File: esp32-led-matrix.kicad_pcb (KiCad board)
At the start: 2 copper layers, 20.5 x 35.5 mm, 20 parts, among them J1 Conn_01x03, J2 Conn_01x03, J4 USB_C_Receptacle_USB2.0_16P, SW1 RESET, U1 ESP32-C6-WROOM-1, U2 USBLC6-2SC6, U3 LM1117DT-3.3

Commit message: process
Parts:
- removed J1: Conn_01x03, Connector_PinHeader_2.54mm:PinHeader_1x03_P2.54mm_Vertical
- added D10: WS2812B, PCM_SparkFun-LED:WS2812_2020, F.Cu at (7.25, 4.00)
- added D100: WS2812B, PCM_SparkFun-LED:WS2812_2020, B.Cu at (29.8, 17.5)
- added D101: WS2812B, PCM_SparkFun-LED:WS2812_2020, B.Cu at (25.2, 17.5)
- added D102: WS2812B, PCM_SparkFun-LED:WS2812_2020, B.Cu at (20.8, 17.5)
- added D103: WS2812B, PCM_SparkFun-LED:WS2812_2020, B.Cu at (16.2, 17.5)
- added D104: WS2812B, PCM_SparkFun-LED:WS2812_2020, B.Cu at (11.8, 17.5)
- added D105: WS2812B, PCM_SparkFun-LED:WS2812_2020, B.Cu at (7.25, 17.5)
- added D106: WS2812B, PCM_SparkFun-LED:WS2812_2020, B.Cu at (7.25, 22.0)
- added D107: WS2812B, PCM_SparkFun-LED:WS2812_2020, B.Cu at (11.8, 22.0)
- added D108: WS2812B, PCM_SparkFun-LED:WS2812_2020, B.Cu at (16.2, 22.0)
- added D109: WS2812B, PCM_SparkFun-LED:WS2812_2020, B.Cu at (20.8, 22.0)
- added D11: WS2812B, PCM_SparkFun-LED:WS2812_2020, F.Cu at (11.8, 4.00)
- added D110: WS2812B, PCM_SparkFun-LED:WS2812_2020, B.Cu at (25.2, 22.0)
- added D111: WS2812B, PCM_SparkFun-LED:WS2812_2020, B.Cu at (29.8, 22.0)
- added D112: WS2812B, PCM_SparkFun-LED:WS2812_2020, B.Cu at (34.2, 22.0)
- added D113: WS2812B, PCM_SparkFun-LED:WS2812_2020, B.Cu at (38.8, 22.0)
- added D114: WS2812B, PCM_SparkFun-LED:WS2812_2020, B.Cu at (38.8, 26.5)
- added D115: WS2812B, PCM_SparkFun-LED:WS2812_2020, B.Cu at (34.2, 26.5)
- added D116: WS2812B, PCM_SparkFun-LED:WS2812_2020, B.Cu at (29.8, 26.5)
- added D117: WS2812B, PCM_SparkFun-LED:WS2812_2020, B.Cu at (25.2, 26.5)
- added D118: WS2812B, PCM_SparkFun-LED:WS2812_2020, B.Cu at (20.8, 26.5)
- added D119: WS2812B, PCM_SparkFun-LED:WS2812_2020, B.Cu at (16.2, 26.5)
- added D12: WS2812B, PCM_SparkFun-LED:WS2812_2020, F.Cu at (16.2, 4.00)
- added D120: WS2812B, PCM_SparkFun-LED:WS2812_2020, B.Cu at (11.8, 26.5)
- added D121: WS2812B, PCM_SparkFun-LED:WS2812_2020, B.Cu at (7.25, 26.5)
- added D122: WS2812B, PCM_SparkFun-LED:WS2812_2020, B.Cu at (7.25, 31.0)
- added D123: WS2812B, PCM_SparkFun-LED:WS2812_2020, B.Cu at (11.8, 31.0)
- added D124: WS2812B, PCM_SparkFun-LED:WS2812_2020, B.Cu at (16.2, 31.0)
- added D125: WS2812B, PCM_SparkFun-LED:WS2812_2020, B.Cu at (20.8, 31.0)
- added D126: WS2812B, PCM_SparkFun-LED:WS2812_2020, B.Cu at (25.2, 31.0)
- added D127: WS2812B, PCM_SparkFun-LED:WS2812_2020, B.Cu at (29.8, 31.0)
- added D128: WS2812B, PCM_SparkFun-LED:WS2812_2020, B.Cu at (34.2, 31.0)
- added D129: WS2812B, PCM_SparkFun-LED:WS2812_2020, B.Cu at (38.8, 31.0)
- added D13: WS2812B, PCM_SparkFun-LED:WS2812_2020, F.Cu at (20.8, 4.00)
- added D130: WS2812B, PCM_SparkFun-LED:WS2812_2020, B.Cu at (38.8, 35.5)
- added D131: WS2812B, PCM_SparkFun-LED:WS2812_2020, B.Cu at (34.2, 35.5)
- added D132: WS2812B, PCM_SparkFun-LED:WS2812_2020, B.Cu at (29.8, 35.5)
- added D133: WS2812B, PCM_SparkFun-LED:WS2812_2020, B.Cu at (25.2, 35.5)
- added D134: WS2812B, PCM_SparkFun-LED:WS2812_2020, B.Cu at (20.8, 35.5)
- added D135: WS2812B, PCM_SparkFun-LED:WS2812_2020, B.Cu at (16.2, 35.5)
- added D136: WS2812B, PCM_SparkFun-LED:WS2812_2020, B.Cu at (11.8, 35.5)
- added D137: WS2812B, PCM_SparkFun-LED:WS2812_2020, B.Cu at (7.25, 35.5)
- added D14: WS2812B, PCM_SparkFun-LED:WS2812_2020, F.Cu at (25.2, 4.00)
- added D15: WS2812B, PCM_SparkFun-LED:WS2812_2020, F.Cu at (29.8, 4.00)
- added D16: WS2812B, PCM_SparkFun-LED:WS2812_2020, F.Cu at (34.2, 4.00)
- added D17: WS2812B, PCM_SparkFun-LED:WS2812_2020, F.Cu at (38.8, 4.00)
- added D18: WS2812B, PCM_SparkFun-LED:WS2812_2020, F.Cu at (38.8, 8.50)
- added D19: WS2812B, PCM_SparkFun-LED:WS2812_2020, F.Cu at (34.2, 8.50)
- added D20: WS2812B, PCM_SparkFun-LED:WS2812_2020, F.Cu at (29.8, 8.50)
- added D21: WS2812B, PCM_SparkFun-LED:WS2812_2020, F.Cu at (25.2, 8.50)
- added D22: WS2812B, PCM_SparkFun-LED:WS2812_2020, F.Cu at (20.8, 8.50)
- added D23: WS2812B, PCM_SparkFun-LED:WS2812_2020, F.Cu at (16.2, 8.50)
- added D24: WS2812B, PCM_SparkFun-LED:WS2812_2020, F.Cu at (11.8, 8.50)
- added D25: WS2812B, PCM_SparkFun-LED:WS2812_2020, F.Cu at (7.25, 8.50)
- added D26: WS2812B, PCM_SparkFun-LED:WS2812_2020, F.Cu at (7.25, 13.0)
- added D27: WS2812B, PCM_SparkFun-LED:WS2812_2020, F.Cu at (11.8, 13.0)
- added D28: WS2812B, PCM_SparkFun-LED:WS2812_2020, F.Cu at (16.2, 13.0)
- added D29: WS2812B, PCM_SparkFun-LED:WS2812_2020, F.Cu at (20.8, 13.0)
- added D30: WS2812B, PCM_SparkFun-LED:WS2812_2020, F.Cu at (25.2, 13.0)
- added D31: WS2812B, PCM_SparkFun-LED:WS2812_2020, F.Cu at (29.8, 13.0)
- added D32: WS2812B, PCM_SparkFun-LED:WS2812_2020, F.Cu at (34.2, 13.0)
- added D33: WS2812B, PCM_SparkFun-LED:WS2812_2020, F.Cu at (38.8, 13.0)
- added D34: WS2812B, PCM_SparkFun-LED:WS2812_2020, F.Cu at (38.8, 17.5)
- added D35: WS2812B, PCM_SparkFun-LED:WS2812_2020, F.Cu at (34.2, 17.5)
- added D36: WS2812B, PCM_SparkFun-LED:WS2812_2020, F.Cu at (29.8, 17.5)
- added D37: WS2812B, PCM_SparkFun-LED:WS2812_2020, F.Cu at (25.2, 17.5)
- added D38: WS2812B, PCM_SparkFun-LED:WS2812_2020, F.Cu at (20.8, 17.5)
- added D39: WS2812B, PCM_SparkFun-LED:WS2812_2020, F.Cu at (16.2, 17.5)
- added D40: WS2812B, PCM_SparkFun-LED:WS2812_2020, F.Cu at (11.8, 17.5)
- added D41: WS2812B, PCM_SparkFun-LED:WS2812_2020, F.Cu at (7.25, 17.5)
- added D42: WS2812B, PCM_SparkFun-LED:WS2812_2020, F.Cu at (7.25, 22.0)
- added D43: WS2812B, PCM_SparkFun-LED:WS2812_2020, F.Cu at (11.8, 22.0)
- added D44: WS2812B, PCM_SparkFun-LED:WS2812_2020, F.Cu at (16.2, 22.0)
- added D45: WS2812B, PCM_SparkFun-LED:WS2812_2020, F.Cu at (20.8, 22.0)
- added D46: WS2812B, PCM_SparkFun-LED:WS2812_2020, F.Cu at (25.2, 22.0)
- added D47: WS2812B, PCM_SparkFun-LED:WS2812_2020, F.Cu at (29.8, 22.0)
- added D48: WS2812B, PCM_SparkFun-LED:WS2812_2020, F.Cu at (34.2, 22.0)
- added D49: WS2812B, PCM_SparkFun-LED:WS2812_2020, F.Cu at (38.8, 22.0)
- added D50: WS2812B, PCM_SparkFun-LED:WS2812_2020, F.Cu at (38.8, 26.5)
- added D51: WS2812B, PCM_SparkFun-LED:WS2812_2020, F.Cu at (34.2, 26.5)
- added D52: WS2812B, PCM_SparkFun-LED:WS2812_2020, F.Cu at (29.8, 26.5)
- added D53: WS2812B, PCM_SparkFun-LED:WS2812_2020, F.Cu at (25.2, 26.5)
- added D54: WS2812B, PCM_SparkFun-LED:WS2812_2020, F.Cu at (20.8, 26.5)
- added D55: WS2812B, PCM_SparkFun-LED:WS2812_2020, F.Cu at (16.2, 26.5)
- added D56: WS2812B, PCM_SparkFun-LED:WS2812_2020, F.Cu at (11.8, 26.5)
- added D57: WS2812B, PCM_SparkFun-LED:WS2812_2020, F.Cu at (7.25, 26.5)
- added D58: WS2812B, PCM_SparkFun-LED:WS2812_2020, F.Cu at (7.25, 31.0)
- added D59: WS2812B, PCM_SparkFun-LED:WS2812_2020, F.Cu at (11.8, 31.0)
- added D60: WS2812B, PCM_SparkFun-LED:WS2812_2020, F.Cu at (16.2, 31.0)
- added D61: WS2812B, PCM_SparkFun-LED:WS2812_2020, F.Cu at (20.8, 31.0)
- added D62: WS2812B, PCM_SparkFun-LED:WS2812_2020, F.Cu at (25.2, 31.0)
- added D63: WS2812B, PCM_SparkFun-LED:WS2812_2020, F.Cu at (29.8, 31.0)
- added D64: WS2812B, PCM_SparkFun-LED:WS2812_2020, F.Cu at (34.2, 31.0)
- added D65: WS2812B, PCM_SparkFun-LED:WS2812_2020, F.Cu at (38.8, 31.0)
- added D66: WS2812B, PCM_SparkFun-LED:WS2812_2020, F.Cu at (38.8, 35.5)
- added D67: WS2812B, PCM_SparkFun-LED:WS2812_2020, F.Cu at (34.2, 35.5)
- added D68: WS2812B, PCM_SparkFun-LED:WS2812_2020, F.Cu at (29.8, 35.5)
- added D69: WS2812B, PCM_SparkFun-LED:WS2812_2020, F.Cu at (25.2, 35.5)
- added D70: WS2812B, PCM_SparkFun-LED:WS2812_2020, F.Cu at (20.8, 35.5)
- added D71: WS2812B, PCM_SparkFun-LED:WS2812_2020, F.Cu at (16.2, 35.5)
- added D72: WS2812B, PCM_SparkFun-LED:WS2812_2020, F.Cu at (11.8, 35.5)
- added D73: WS2812B, PCM_SparkFun-LED:WS2812_2020, F.Cu at (7.25, 35.5)
- added D74: WS2812B, PCM_SparkFun-LED:WS2812_2020, B.Cu at (7.25, 4.00)
- added D75: WS2812B, PCM_SparkFun-LED:WS2812_2020, B.Cu at (11.8, 4.00)
- added D76: WS2812B, PCM_SparkFun-LED:WS2812_2020, B.Cu at (16.2, 4.00)
- added D77: WS2812B, PCM_SparkFun-LED:WS2812_2020, B.Cu at (20.8, 4.00)
- added D78: WS2812B, PCM_SparkFun-LED:WS2812_2020, B.Cu at (25.2, 4.00)
- added D79: WS2812B, PCM_SparkFun-LED:WS2812_2020, B.Cu at (29.8, 4.00)
- added D80: WS2812B, PCM_SparkFun-LED:WS2812_2020, B.Cu at (34.2, 4.00)
- added D81: WS2812B, PCM_SparkFun-LED:WS2812_2020, B.Cu at (38.8, 4.00)
- added D82: WS2812B, PCM_SparkFun-LED:WS2812_2020, B.Cu at (38.8, 8.50)
- added D83: WS2812B, PCM_SparkFun-LED:WS2812_2020, B.Cu at (34.2, 8.50)
- added D84: WS2812B, PCM_SparkFun-LED:WS2812_2020, B.Cu at (29.8, 8.50)
- added D85: WS2812B, PCM_SparkFun-LED:WS2812_2020, B.Cu at (25.2, 8.50)
- added D86: WS2812B, PCM_SparkFun-LED:WS2812_2020, B.Cu at (20.8, 8.50)
- added D87: WS2812B, PCM_SparkFun-LED:WS2812_2020, B.Cu at (16.2, 8.50)
- added D88: WS2812B, PCM_SparkFun-LED:WS2812_2020, B.Cu at (11.8, 8.50)
- added D89: WS2812B, PCM_SparkFun-LED:WS2812_2020, B.Cu at (7.25, 8.50)
- added D90: WS2812B, PCM_SparkFun-LED:WS2812_2020, B.Cu at (7.25, 13.0)
- added D91: WS2812B, PCM_SparkFun-LED:WS2812_2020, B.Cu at (11.8, 13.0)
- added D92: WS2812B, PCM_SparkFun-LED:WS2812_2020, B.Cu at (16.2, 13.0)
- added D93: WS2812B, PCM_SparkFun-LED:WS2812_2020, B.Cu at (20.8, 13.0)
- added D94: WS2812B, PCM_SparkFun-LED:WS2812_2020, B.Cu at (25.2, 13.0)
- added D95: WS2812B, PCM_SparkFun-LED:WS2812_2020, B.Cu at (29.8, 13.0)
- added D96: WS2812B, PCM_SparkFun-LED:WS2812_2020, B.Cu at (34.2, 13.0)
- added D97: WS2812B, PCM_SparkFun-LED:WS2812_2020, B.Cu at (38.8, 13.0)
- added D98: WS2812B, PCM_SparkFun-LED:WS2812_2020, B.Cu at (38.8, 17.5)
- added D99: WS2812B, PCM_SparkFun-LED:WS2812_2020, B.Cu at (34.2, 17.5)
- J2: value Conn_01x03 -> Conn_01x04; footprint Connector_PinHeader_2.54mm:PinHeader_1x03_P2.54mm_Vertical -> PCM_SparkFun-Connector:JST_1x04_P2.0mm_Horizontal_SMD; moved to F.Cu
- moved J2 110.6 mm to (23.0, 83.0), turned to 90 degrees
- moved C1 107.7 mm to (19.2, 59.2)
- moved C2 107.7 mm to (16.7, 59.3)
- moved C3 107.7 mm to (16.7, 57.0)
- moved C5 107.7 mm to (29.2, 51.0)
- moved C6 107.7 mm to (27.7, 50.2)
- moved D1 107.7 mm to (18.2, 53.0)
- moved D4 107.7 mm to (27.2, 46.5)
- moved J4 107.7 mm to (18.7, 70.5)
- moved R1 107.7 mm to (20.2, 70.0)
- moved R2 107.7 mm to (17.2, 70.0)
- moved R7 107.7 mm to (28.7, 47.2)
- moved SW1 107.7 mm to (21.7, 47.0)
- moved U1 107.7 mm to (23.0, 54.8)
- moved U2 107.7 mm to (19.2, 63.0)
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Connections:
- J2 pad 2: Net-(J2-Pad2) -> LEDA_DATA
- J2 pad 3: GND -> LEDB_DATA
- U1 pad 6: unconnected-(U1-MTCK/GPIO6/ADC1_CH6-Pad6) -> LEDA_DATA
- U1 pad 7: unconnected-(U1-MTDO/GPIO7-Pad7) -> LEDB_DATA
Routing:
- net Net-(J1-Pad2): track 24.4 -> 0.00 mm
- net Net-(J2-Pad2): track 18.0 -> 0.00 mm
- added copper zone on B.Cu, net +5V
- added copper zone on F.Cu, net +5V
- added copper zone on F.Cu, net GND
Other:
- board size 20.5 x 35.5 mm -> 46 x 91 mm

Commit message: progress
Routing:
- net +5V: track 30.7 -> 25.2 mm
- net GND: track 58.6 -> 58.5 mm, vias 3 -> 1

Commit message: progress
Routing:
- net LEDA_DATA: track 0.00 -> 100.7 mm, vias 0 -> 2
- net LEDB_DATA: track 0.00 -> 32.3 mm, vias 0 -> 1
- net Net-(D49-DOUT): track 0.00 -> 7.21 mm
- net Net-(D33-DOUT): track 0.00 -> 7.21 mm
- net Net-(D17-DOUT): track 0.00 -> 7.21 mm
- net Net-(D57-DOUT): track 0.00 -> 7.21 mm
- net Net-(D41-DOUT): track 0.00 -> 7.21 mm
- net Net-(D25-DOUT): track 0.00 -> 7.21 mm
- net Net-(D125-DOUT): track 0.00 -> 6.08 mm
- net Net-(D65-DOUT): track 0.00 -> 5.76 mm
- net Net-(D108-DOUT): track 0.00 -> 5.65 mm
- net Net-(D121-DOUT): track 0.00 -> 5.49 mm
- net Net-(D89-DOUT): track 0.00 -> 5.13 mm
- net Net-(D129-DOUT): track 0.00 -> 5.13 mm
- net Net-(D105-DOUT): track 0.00 -> 5.13 mm
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
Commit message: progress
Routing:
- net LEDB_DATA: track 32.3 -> 96.7 mm
- net LEDA_DATA: track 100.7 -> 126.7 mm, vias 2 -> 1
- net Net-(D123-DOUT): track 3.13 -> 10.3 mm
- net Net-(D108-DOUT): track 5.65 -> 3.13 mm
- net Net-(D125-DOUT): track 6.08 -> 8.19 mm, vias 0 -> 2
- net Net-(D25-DOUT): track 7.21 -> 5.29 mm
- net Net-(D49-DOUT): track 7.21 -> 5.29 mm
- net Net-(D33-DOUT): track 7.21 -> 5.29 mm
- net Net-(D17-DOUT): track 7.21 -> 5.29 mm
- net Net-(D57-DOUT): track 7.21 -> 5.29 mm
- net Net-(D41-DOUT): track 7.21 -> 5.29 mm
- net Net-(D121-DOUT): track 5.49 -> 4.97 mm

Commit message: progress
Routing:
- net LEDB_DATA: track 96.7 -> 32.5 mm
- net LEDA_DATA: track 126.7 -> 96.6 mm, vias 1 -> 2
- net Net-(D123-DOUT): track 10.3 -> 3.13 mm
- net +5V: track 25.2 -> 30.7 mm
- net Net-(D125-DOUT): track 8.19 -> 3.13 mm, vias 2 -> 0
- net Net-(D124-DOUT): track 3.13 -> 5.29 mm
- net GND: track 58.5 -> 58.6 mm, vias 1 -> 3

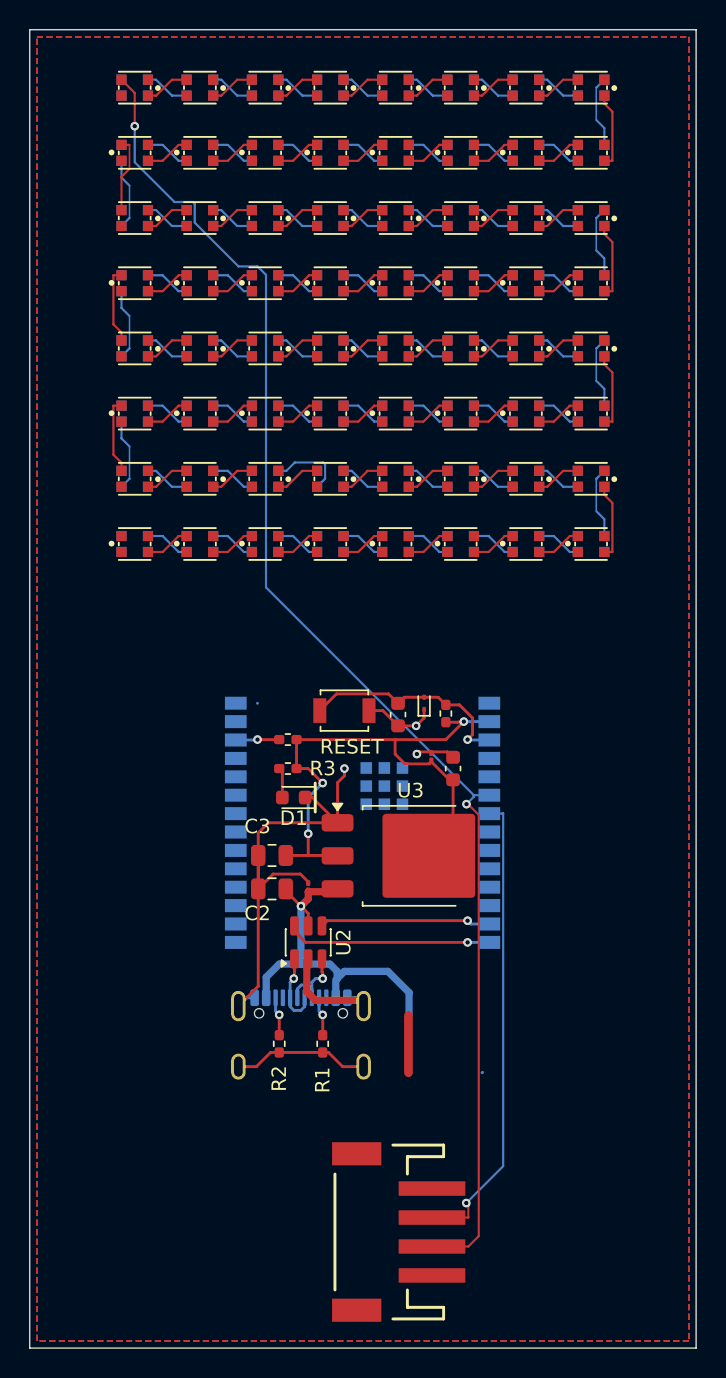
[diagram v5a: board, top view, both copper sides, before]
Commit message: Fix broken PCB routing via Freerouting autorouter; add BOM/fab-files/docs/README
- Cleared all hand-routed copper (577 traces, all shorted/crossing) and
  re-routed via the Freerouting autorouter (v2.1.0, Java-21 compatible
  build — v2.4.1 shipped requires Java 25 which isn't installed)
- Fixed GND/+5V zone priority bug: both power-pour zones defaulted to
  overlapping full-board fills with +5V outranking GND, starving GND
  fill to near-zero; swapped priorities and added connect_pads=yes for
  solid (non-thermal-relief) GND pad connections
- Added ~700 GND stitching vias (F.Cu<->B.Cu pour bridging) across
  several tuned passes, removing colliding/clearance-violating ones
- Re-ran Freerouting standalone (DSN/SES) for the +5V point-to-point
  net after removing the competing +5V zones, closing 27 of 47
  originally-unrouted +5V segments
- DRC: 376 violations / 267 unconnected -> 100 violations (all
  pre-existing benign lib_footprint_mismatch) / 61 unconnected
  (GND/+5V power-net pour gaps only -- all 128 LED data-chain nets on
  GPIO6/GPIO7 are 100% routed with 0 unconnected)
- ERC: 78 violations, confirmed matches documented benign baseline
  (unused GPIO/USB pins, 2 expected chain-end dangling labels)
- Added BOM_jlcpcb_verified.csv (every line LCSC-populated, sourced
  from schematic properties via kicad-cli sch export bom)
- Added production/ fab package: gerbers.zip, drill, bom.csv (JLCPCB
  format), positions.csv (CPL, both sides)
- Added docs/images/: schematic PDF+PNG, PCB layout PNG, 3D renders
  (top/bottom/isometric)
- Added README.md documenting board specs, BOM, manufacturing,
  DRC/ERC status, repo layout
- Added .gitignore for .mcp-backups/ and scratch diagnostic files;
  removed a previously-tracked .mcp-backups/ file from git
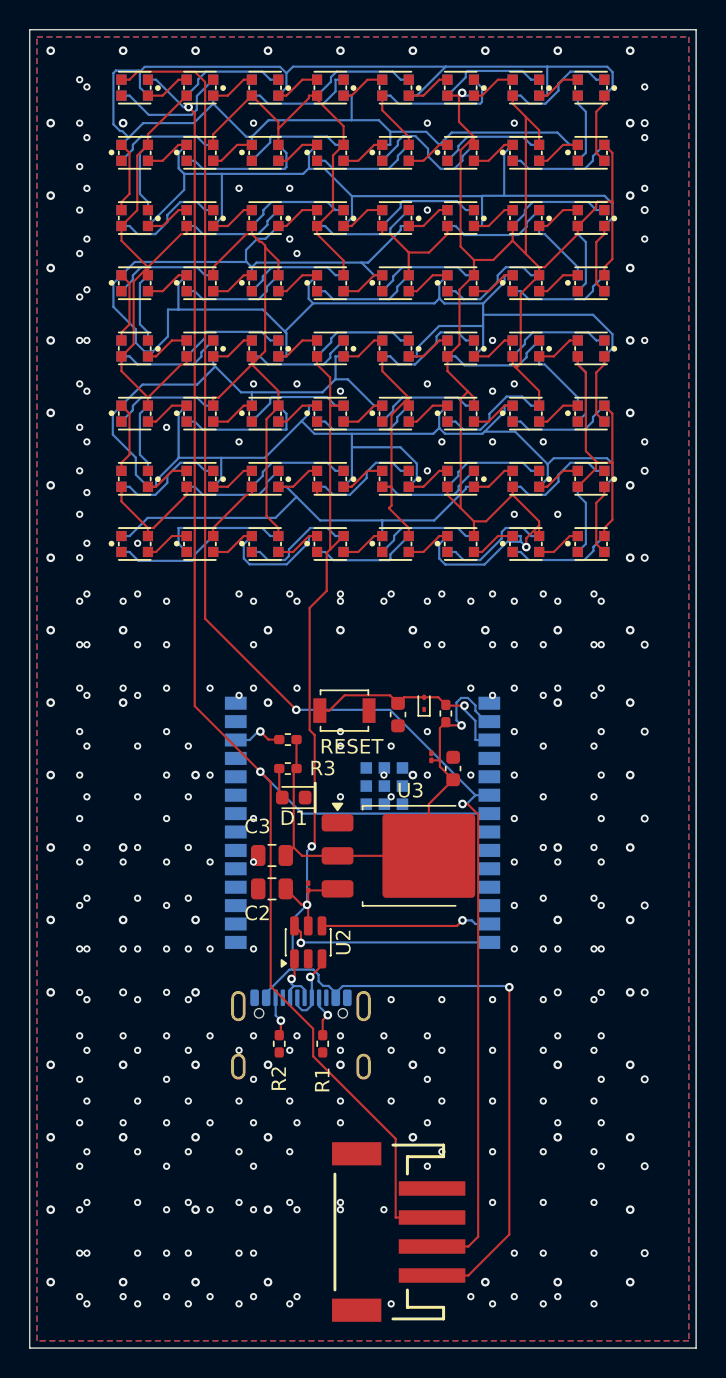
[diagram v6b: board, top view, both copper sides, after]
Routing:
- net +5V: track 30.7 -> 748.8 mm, vias 1 -> 5
- net LEDB_DATA: track 32.5 -> 105.7 mm, vias 1 -> 2
- net GND: track 58.6 -> 0.00 mm, vias 3 -> 381
- net LEDA_DATA: track 96.6 -> 103.1 mm
- net Net-(D84-DOUT): track 3.13 -> 9.30 mm
- net Net-(D135-DOUT): track 3.13 -> 9.00 mm
- net Net-(D119-DOUT): track 3.13 -> 9.00 mm
- net Net-(D78-DOUT): track 3.13 -> 8.93 mm
- net Net-(D87-DOUT): track 3.13 -> 8.93 mm
- net Net-(D74-DOUT): track 3.13 -> 8.44 mm
- net +3V3: track 40.2 -> 35.1 mm, vias 3 -> 1
- net Net-(D115-DOUT): track 3.13 -> 8.05 mm
- net Net-(D80-DOUT): track 3.13 -> 8.00 mm
- net Net-(D90-DOUT): track 3.13 -> 8.00 mm
- net Net-(D128-DOUT): track 3.13 -> 8.00 mm
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- removed copper zone on B.Cu, net +5V
- removed copper zone on F.Cu, net +5V
